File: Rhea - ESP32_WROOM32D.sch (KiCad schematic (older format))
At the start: 9 parts

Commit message: Power management updates.
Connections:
- net USB_DATA+ renamed Power Management/USB_DATAP_IN
- net USB_DATA- renamed Power Management/USB_DATAN_IN
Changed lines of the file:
@@
 $EndDescr
 $Sheet
-S 1600 3050 1400 1000
+S 1600 3050 1400 1250
 U 5E2B3D45
 F0 "Power Management" 50
 F1 "pwr_mgmt.sch" 50
-F2 "~CHARGING" O R 3000 3925 50
-F3 "POWER_ON" O R 3000 3800 50
+F2 "~CHARGING" O R 3000 4025 50
+F3 "POWER_ON" O R 3000 3925 50
 F4 "USB_5V" I L 1600 3150 50
 F5 "I2C" B R 3000 3425 50
 F6 "POWER_OUT" O R 3000 3175 50
+F7 "USB_DATA+" O R 3000 4125 50
+F8 "USB_DATA-" O R 3000 4225 50
+F9 "USB_DATAP_IN" I L 1600 3350 50
+F10 "USB_DATAN_IN" I L 1600 3450 50
 $EndSheet
 $Comp
@@
 L Graphic:SYM_Flash_Large #SYM?
 U 1 1 5E2D7EF8
-P 2275 3550
-F 0 "#SYM?" V 2125 3550 50  0001 C CNN
-F 1 "SYM_Flash_Large" V 2405 3550 50  0001 C CNN
-F 2 "" H 2265 3460 50  0001 C CNN
-F 3 "~" H 2675 3450 50  0001 C CNN
-	1    2275 3550
-	1    0    0    -1
-$EndComp
-Text Notes 1600 4275 0    50   ~ 0
+P 2300 3675
+F 0 "#SYM?" V 2150 3675 50  0001 C CNN
+F 1 "SYM_Flash_Large" V 2430 3675 50  0001 C CNN
+F 2 "" H 2290 3585 50  0001 C CNN
+F 3 "~" H 2700 3575 50  0001 C CNN
+	1    2300 3675
+	1    0    0    -1
+$EndComp
+Text Notes 1600 4500 0    50   ~ 0
 Overcurrent & Overvoltage protection
-Text Notes 1600 4475 0    50   ~ 0
+Text Notes 1600 4700 0    50   ~ 0
 Buck Converter + LDO
-Text Notes 1600 4375 0    50   ~ 0
+Text Notes 1600 4600 0    50   ~ 0
 Current-feedback protection
-Text Notes 1600 4575 0    50   ~ 0
+Text Notes 1600 4800 0    50   ~ 0
 Power monitoring
-Text Notes 1600 4675 0    50   ~ 0
+Text Notes 1600 4900 0    50   ~ 0
 Power-on reset
-Text Notes 1600 4775 0    50   ~ 0
+Text Notes 1600 5000 0    50   ~ 0
 Li-Ion Battery Charger
 Text Label 3825 3175 2    50   ~ 0
@@
 	1    0    0    -1
 $EndComp
-Text HLabel 1100 3350 2    50   Output ~ 0
-USB_DATA+
-Text HLabel 1100 3450 2    50   Output ~ 0
-USB_DATA-
-Wire Wire Line
-	1075 3350 1100 3350
-Wire Wire Line
-	1075 3450 1100 3450
 Wire Wire Line
 	1075 3150 1600 3150
@@
 Text Notes 7075 1050 2    100  ~ 20
 Grounds
+Wire Wire Line
+	1075 3350 1600 3350
+Wire Wire Line
+	1075 3450 1600 3450
 Wire Bus Line
 	9700 1975 9700 3425
 Wire Bus Line
+	4150 3550 4150 7025
+Wire Bus Line
 	3275 3425 3275 6675
-Wire Bus Line
-	4150 3550 4150 7025
 $EndSCHEMATC

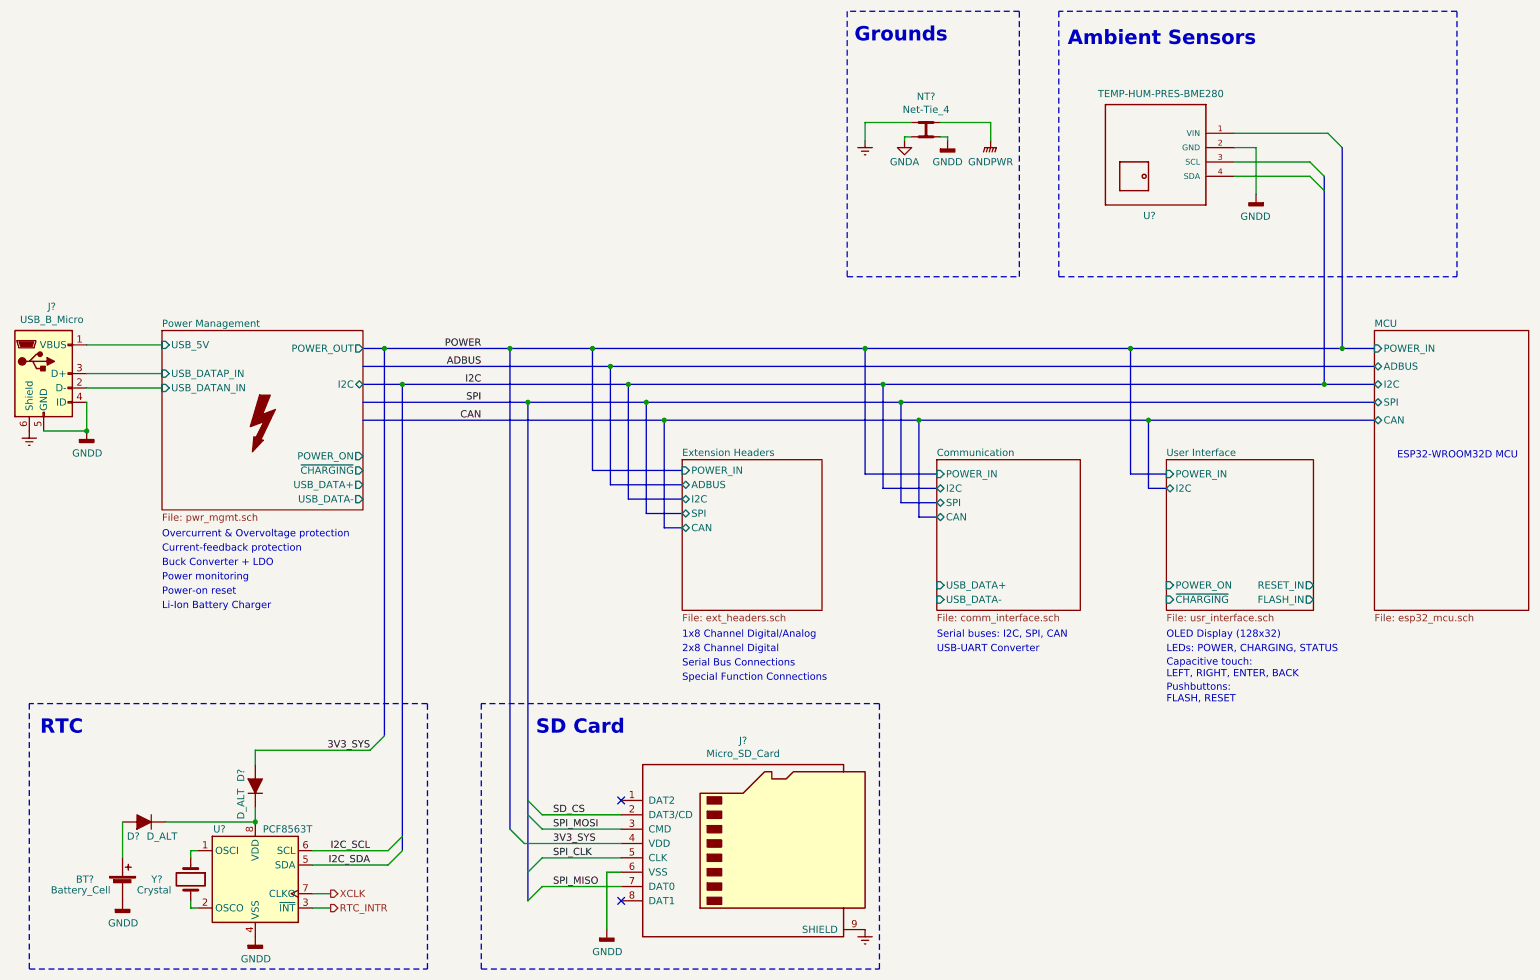
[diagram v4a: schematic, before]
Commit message: Automatic charge source selection & Documentation updates.
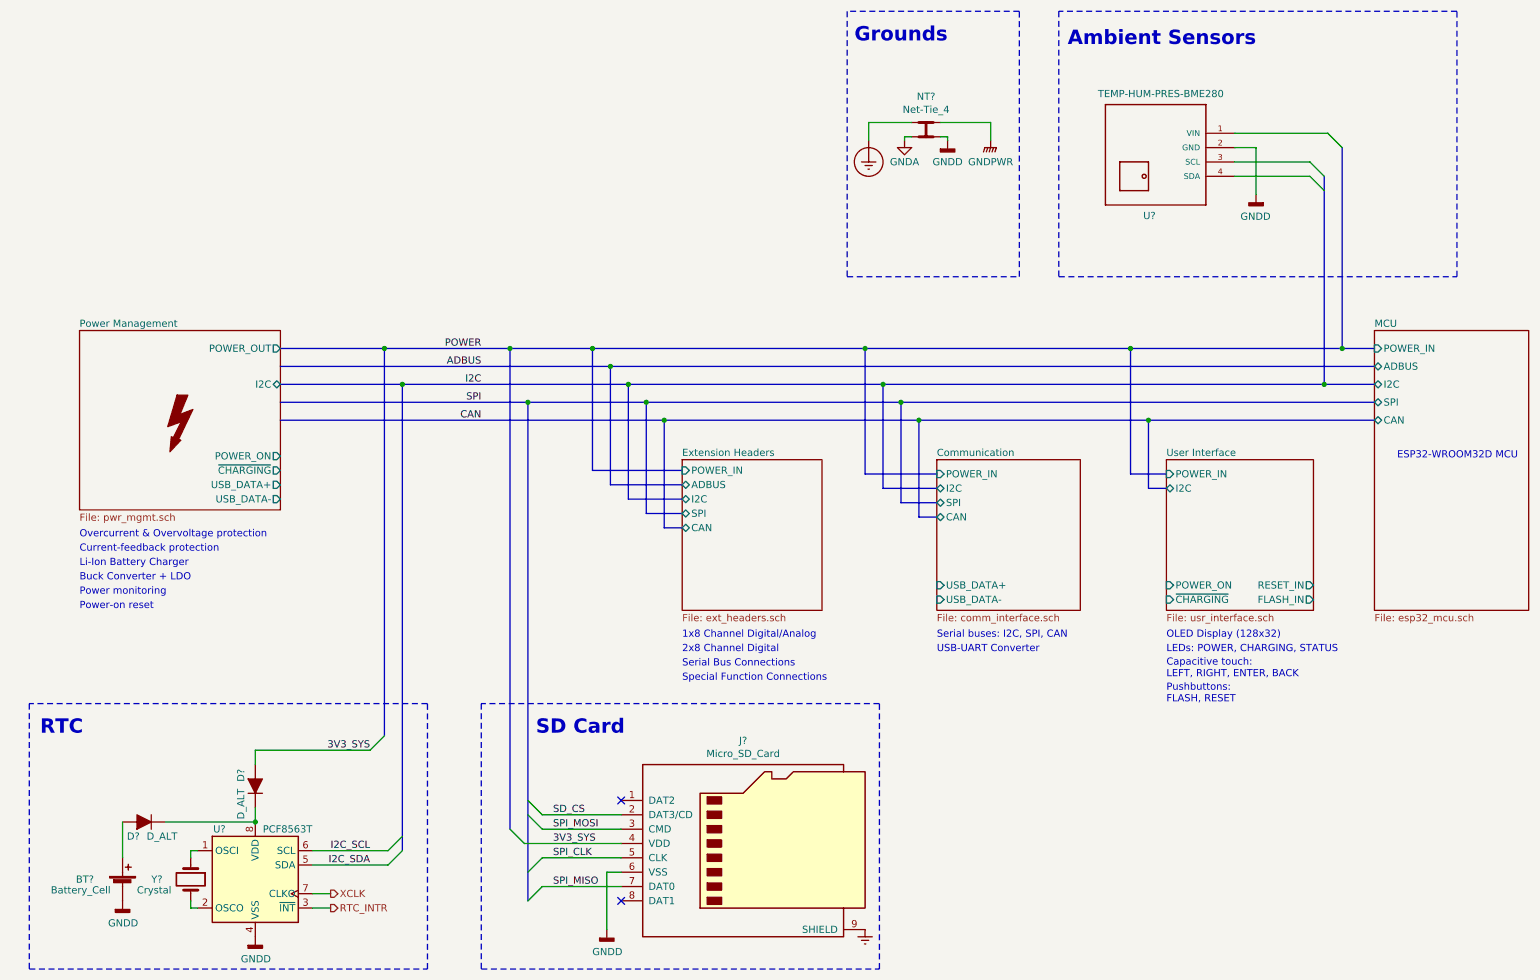
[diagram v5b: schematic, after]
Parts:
- removed J?: USB_B_Micro, symbol Connector:USB_B_Micro
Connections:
- net Earth: no longer NT?.1
- new net Earth_Protective: NT?.1
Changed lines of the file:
@@
 $EndDescr
 $Sheet
-S 1600 3050 1400 1250
+S 1025 3050 1400 1250
 U 5E2B3D45
 F0 "Power Management" 50
 F1 "pwr_mgmt.sch" 50
-F2 "~CHARGING" O R 3000 4025 50
-F3 "POWER_ON" O R 3000 3925 50
-F4 "USB_5V" I L 1600 3150 50
-F5 "I2C" B R 3000 3425 50
-F6 "POWER_OUT" O R 3000 3175 50
-F7 "USB_DATA+" O R 3000 4125 50
-F8 "USB_DATA-" O R 3000 4225 50
-F9 "USB_DATAP_IN" I L 1600 3350 50
-F10 "USB_DATAN_IN" I L 1600 3450 50
+F2 "~CHARGING" O R 2425 4025 50
+F3 "POWER_ON" O R 2425 3925 50
+F4 "I2C" B R 2425 3425 50
+F5 "POWER_OUT" O R 2425 3175 50
+F6 "USB_DATA+" O R 2425 4125 50
+F7 "USB_DATA-" O R 2425 4225 50
 $EndSheet
-$Comp
-L Connector:USB_B_Micro J?
-U 1 1 5E2CF1FC
-P 775 3350
-F 0 "J?" H 832 3817 50  0000 C CNN
-F 1 "USB_B_Micro" H 832 3726 50  0000 C CNN
-F 2 "" H 925 3300 50  0001 C CNN
-F 3 "~" H 925 3300 50  0001 C CNN
-	1    775  3350
-	1    0    0    -1
-$EndComp
 $Comp
 L Graphic:SYM_Flash_Large #SYM?
 U 1 1 5E2D7EF8
-P 2300 3675
-F 0 "#SYM?" V 2150 3675 50  0001 C CNN
-F 1 "SYM_Flash_Large" V 2430 3675 50  0001 C CNN
-F 2 "" H 2290 3585 50  0001 C CNN
-F 3 "~" H 2700 3575 50  0001 C CNN
-	1    2300 3675
-	1    0    0    -1
-$EndComp
-Text Notes 1600 4500 0    50   ~ 0
+P 1725 3675
+F 0 "#SYM?" V 1575 3675 50  0001 C CNN
+F 1 "SYM_Flash_Large" V 1855 3675 50  0001 C CNN
+F 2 "" H 1715 3585 50  0001 C CNN
+F 3 "~" H 2125 3575 50  0001 C CNN
+	1    1725 3675
+	1    0    0    -1
+$EndComp
+Text Notes 1025 4500 0    50   ~ 0
 Overcurrent & Overvoltage protection
-Text Notes 1600 4700 0    50   ~ 0
+Text Notes 1025 4800 0    50   ~ 0
 Buck Converter + LDO
-Text Notes 1600 4600 0    50   ~ 0
+Text Notes 1025 4600 0    50   ~ 0
 Current-feedback protection
-Text Notes 1600 4800 0    50   ~ 0
+Text Notes 1025 4900 0    50   ~ 0
 Power monitoring
-Text Notes 1600 4900 0    50   ~ 0
+Text Notes 1025 5000 0    50   ~ 0
 Power-on reset
-Text Notes 1600 5000 0    50   ~ 0
+Text Notes 1025 4700 0    50   ~ 0
 Li-Ion Battery Charger
 Text Label 3825 3175 2    50   ~ 0
@@
 	1    0    0    -1
 $EndComp
-Wire Wire Line
-	1075 3150 1600 3150
 $Comp
 L Connector:Micro_SD_Card J?
@@
 	1    0    0    -1
 $EndComp
-$Comp
-L power:Earth #PWR0106
-U 1 1 5E2D2975
-P 675 3750
-F 0 "#PWR0106" H 675 3500 50  0001 C CNN
-F 1 "Earth" H 675 3600 50  0001 C CNN
-F 2 "" H 675 3750 50  0001 C CNN
-F 3 "~" H 675 3750 50  0001 C CNN
-	1    675  3750
-	1    0    0    -1
-$EndComp
-$Comp
-L power:GNDD #PWR0107
-U 1 1 5E2D346A
-P 1075 3750
-F 0 "#PWR0107" H 1075 3500 50  0001 C CNN
-F 1 "GNDD" H 1079 3595 50  0000 C CNN
-F 2 "" H 1075 3750 50  0001 C CNN
-F 3 "" H 1075 3750 50  0001 C CNN
-	1    1075 3750
-	1    0    0    -1
-$EndComp
-Wire Wire Line
-	1075 3550 1075 3750
-Wire Wire Line
-	775  3750 1075 3750
-Connection ~ 1075 3750
 $Comp
 L power:GNDD #PWR0108
@@
 Data
 89 50 4E 47 0D 0A 1A 0A 00 00 00 0D 49 48 44 52 00 00 00 82 00 00 00 82 08 03 00 00 00 BD DD E0
-CF 00 00 00 03 73 42 49 54 08 08 08 DB E1 4F E0 00 00 00 30 50 4C 54 45 02 00 00 EB EB EB 61 61
+CF 00 00 00 03 73 42 49 54 08 08 08 DB E1 4F E0 00 00 00 30 50 4C 54 45 01 00 00 EB EB EB 61 61
 61 FE FE FE 4F 4F 4F 00 00 00 32 32 32 F3 F3 F3 1B 1B 1B E4 E4 E4 FD FD FD 0A 0A 0A CB CB CB FF
-FF FF 7C 7C 7C A7 A7 A7 ED 50 FD 35 00 00 00 01 74 52 4E 53 00 40 E6 D8 66 00 00 00 B4 49 44 41
+FF FF 7C 7C 7C A7 A7 A7 AB 82 C8 51 00 00 00 01 74 52 4E 53 00 40 E6 D8 66 00 00 00 B4 49 44 41
 54 78 9C ED D6 B9 0E C3 40 08 45 D1 71 66 F0 BE FC FF DF BA 48 6C 09 57 14 09 10 E9 9E EA 15 2E
 90 3C 2C A5 00 00 00 00 00 00 00 00 80 87 EE 55 1F C1 5D 93 7E D0 C1 DD D0 CB 38 A9 E0 6F 6E B2
@@
 Special Function Connections
 Wire Bus Line
-	3000 3425 3275 3425
-Wire Bus Line
-	3000 3175 3150 3175
-Wire Bus Line
-	3000 3300 4725 3300
-Wire Bus Line
-	3000 3550 4150 3550
-Wire Bus Line
-	3000 3675 5100 3675
-Wire Bus Line
 	3150 3175 3150 5875
 Connection ~ 3150 3175
@@
 	1    0    0    -1
 $EndComp
-$Comp
-L power:Earth #PWR0112
-U 1 1 5E3BDC81
-P 6500 1725
-F 0 "#PWR0112" H 6500 1475 50  0001 C CNN
-F 1 "Earth" H 6500 1575 50  0001 C CNN
-F 2 "" H 6500 1725 50  0001 C CNN
-F 3 "~" H 6500 1725 50  0001 C CNN
-	1    6500 1725
-	1    0    0    -1
-$EndComp
 Wire Wire Line
 	7375 1725 7375 1600
@@
 	7375 1600 7025 1600
 Wire Wire Line
-	6500 1600 6500 1725
-Wire Wire Line
-	6500 1600 6825 1600
+	6525 1600 6525 1725
 Wire Notes Line
 	7575 2675 7575 825
@@
 Text Notes 7075 1050 2    100  ~ 20
 Grounds
-Wire Wire Line
-	1075 3350 1600 3350
-Wire Wire Line
-	1075 3450 1600 3450
+$Comp
+L power:Earth_Protective #PWR?
+U 1 1 5E63B8FE
+P 6525 1725
+F 0 "#PWR?" H 6775 1475 50  0001 C CNN
+F 1 "Earth_Protective" H 6975 1575 50  0001 C CNN
+F 2 "" H 6525 1625 50  0001 C CNN
+F 3 "~" H 6525 1625 50  0001 C CNN
+	1    6525 1725
+	1    0    0    -1
+$EndComp
+Wire Wire Line
+	6525 1600 6825 1600
+Wire Bus Line
+	2425 3175 3150 3175
+Wire Bus Line
+	2425 3425 3275 3425
+Wire Bus Line
+	2425 3300 4725 3300
+Wire Bus Line
+	2425 3550 4150 3550
+Wire Bus Line
+	2425 3675 5100 3675
 Wire Bus Line
 	9700 1975 9700 3425

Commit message: External headers early draft.
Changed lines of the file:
@@
 $Bitmap
 Pos 5775 4350
-Scale 1.000000
+Scale 2.000000
 Data
-89 50 4E 47 0D 0A 1A 0A 00 00 00 0D 49 48 44 52 00 00 00 82 00 00 00 82 08 03 00 00 00 BD DD E0
-CF 00 00 00 03 73 42 49 54 08 08 08 DB E1 4F E0 00 00 00 30 50 4C 54 45 01 00 00 EB EB EB 61 61
-61 FE FE FE 4F 4F 4F 00 00 00 32 32 32 F3 F3 F3 1B 1B 1B E4 E4 E4 FD FD FD 0A 0A 0A CB CB CB FF
-FF FF 7C 7C 7C A7 A7 A7 AB 82 C8 51 00 00 00 01 74 52 4E 53 00 40 E6 D8 66 00 00 00 B4 49 44 41
-54 78 9C ED D6 B9 0E C3 40 08 45 D1 71 66 F0 BE FC FF DF BA 48 6C 09 57 14 09 10 E9 9E EA 15 2E
-90 3C 2C A5 00 00 00 00 00 00 00 00 80 87 EE 55 1F C1 5D 93 7E D0 C1 DD D0 CB 38 A9 E0 6F 6E B2
-AC 2A F8 DB 76 91 43 85 00 87 C8 BE A9 E0 6F 5D A4 CD 2A F8 9B C6 4F 3F DC E1 9B C4 EC 5D 8C F1
-BB 3F 2B C1 E4 B7 3F C2 22 FE 39 86 37 65 FC 68 AA D7 5C AE 51 03 3A C1 9A 4A B0 AC 13 9C 2C 48
-22 C1 5B 48 D0 11 09 E6 02 E7 EB 25 7C 53 96 0C F7 02 E7 AB 47 09 26 9C AF 09 9A 32 7E 34 71 BE
-96 14 CB 3A C1 C9 02 00 00 00 00 00 00 00 00 2C 4E 51 2A 0E E9 A9 0D 7E B5 00 00 00 00 49 45 4E
-44 AE 42 60 82
+89 50 4E 47 0D 0A 1A 0A 00 00 00 0D 49 48 44 52 00 00 00 82 00 00 00 82 08 06 00 00 00 8A 03 10
+FD 00 00 00 04 73 42 49 54 08 08 08 08 7C 08 64 88 00 00 02 9A 49 44 41 54 78 9C ED DA BD B1 9B
+40 14 40 E1 83 43 5A 40 55 A8 11 5A B0 FA A0 1F 8A 51 19 26 B2 42 62 B8 0E 7C AD B1 07 D9 46 B6
+D0 BE 81 F3 CD DC 6C 83 9D E1 E8 87 85 AA 42 82 4F A5 37 A0 8F C1 10 04 18 82 92 21 08 30 04 25
+43 10 60 08 4A 86 20 C0 10 94 0C 41 80 21 28 19 82 00 43 50 32 04 01 86 A0 64 08 02 0C 41 C9 10
+04 18 82 92 21 08 30 04 25 43 10 60 08 4A 86 20 C0 10 94 0C 41 80 21 28 19 82 00 43 50 32 04 01
+86 A0 64 08 02 0C 41 C9 10 04 18 82 92 21 08 30 04 25 43 10 60 08 4A 86 20 C0 10 94 0C 41 80 21
+28 19 82 80 9D 87 F0 F5 76 8B CF 97 4B 4C F3 1C FF B3 E6 10 AA 1D 4F DB B6 01 C4 F9 7C 8E 71 1C
+E3 5F D7 1C 61 8A 6F 60 CB 19 C7 31 CE E7 73 00 D1 34 4D 0C C3 B0 B8 D0 6B D6 1C 61 8A 6F 60 EB
+99 A6 29 7E 7C EA EB BA 8E EB F5 BA B8 D0 6B D6 EC 7D 8A 6F E0 1D 13 11 D1 75 5D 00 01 44 DF F7
+8B 0B BD 66 CD 9E A7 F8 06 DE 39 7D DF DF 2F 74 D7 75 11 11 8B 8B BD 66 CD 1E A7 F8 06 DE 3D D7
+EB 35 EA BA 0E 20 DA B6 8D 69 9A 16 17 7A CD 9A BD 4D F1 0D 94 98 61 18 A2 69 9A 3F DE 2D AC 59
+B3 AB A9 D8 56 7C FF 9A FD F0 AA FC 60 FC EC CB 30 C4 E9 74 2A B1 9D 85 47 FB 7B A5 5D 1F 28 E9
+09 C5 BF 92 0A 8C 3F 0D CB 29 BE 81 77 8F 7F 16 0D C1 DB C7 A3 87 E0 81 92 21 30 CF F3 5F 8F 8F
+D7 AC D9 FB 14 DF C0 96 E3 43 27 43 A0 C2 C7 D0 86 90 73 BB DD E2 72 B9 C4 3C CF BF BD C0 6B D6
+1C 62 2A 24 4F 16 95 0C 41 C0 CE 43 F0 E5 D5 27 14 FF 93 B2 E1 78 D7 B0 7E 8A 6F 60 CB F1 1C C1
+10 EE E3 CB AB 86 70 1F 9F 35 18 C2 2F E3 D3 47 43 B8 8F EF 23 18 C2 7D 7C 43 E9 C1 54 6C CB 97
+57 5F E3 D1 FE 5E 69 D7 07 4A 7A 42 F1 AF A4 02 E3 4F C3 72 8A 6F E0 DD E3 9F 45 43 F0 F6 F1 E8
+21 78 A0 64 08 BE BC 6A 08 3E 74 32 84 1C 1F 43 1B 02 15 BE BC FA D4 54 48 9E 2C 2A 19 82 00 43
+50 32 04 01 86 A0 64 08 02 0C 41 C9 10 04 18 82 92 21 08 30 04 25 43 10 60 08 4A 86 20 C0 10 94
+0C 41 80 21 28 19 82 00 43 50 32 04 01 86 A0 64 08 02 0C 41 C9 10 04 18 82 92 21 08 30 04 25 43
+10 60 08 4A 86 20 C0 10 94 0C 41 80 21 28 19 82 00 43 50 32 04 01 86 A0 64 08 02 0C 41 C9 10 04
+18 82 92 21 08 30 04 25 43 10 60 08 4A DF 00 16 AF CE FF 61 C4 20 00 00 00 00 00 49 45 4E 44 AE
+42 60 82
 EndData
 $EndBitmap
@@
 F5 "SPI" B L 5225 4325 50
 F6 "POWER_IN" I L 5225 4025 50
+F7 "DIO_INTR" O R 6200 4925 50
 $EndSheet
 Wire Bus Line
